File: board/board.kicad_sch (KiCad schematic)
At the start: 25 parts, among them J1 Conn_01x10_Pin, J2 Conn_01x10, J3 Conn_01x20, J4 Conn_01x02, J5 Conn_01x06, U1 nPM1300-CAXX, U2 ${ISP_PART}

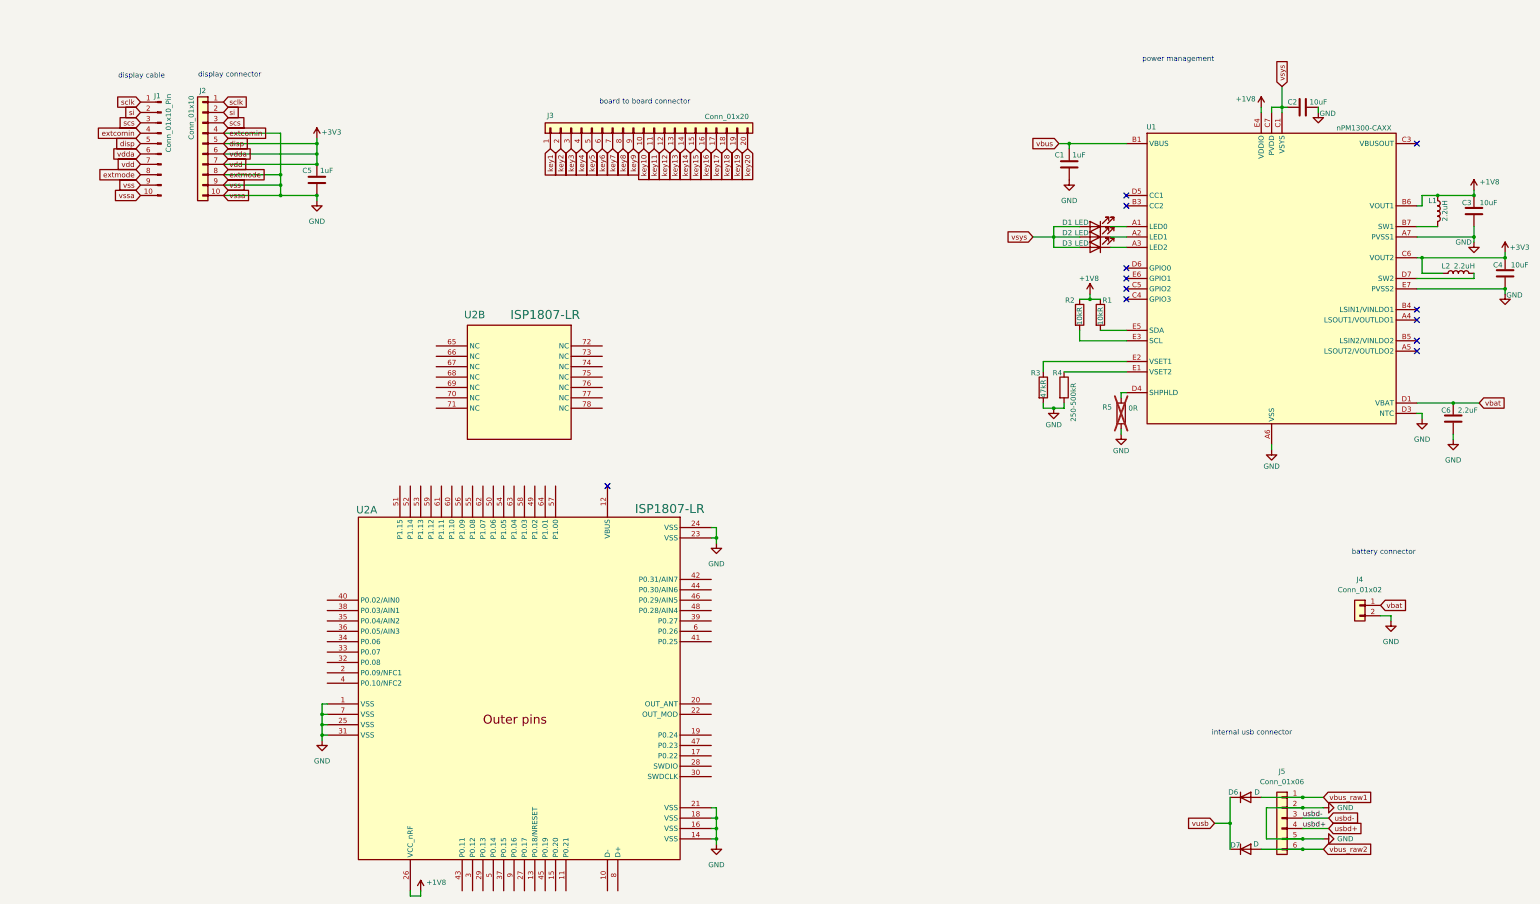
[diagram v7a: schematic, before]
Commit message: board: sch configure vusb
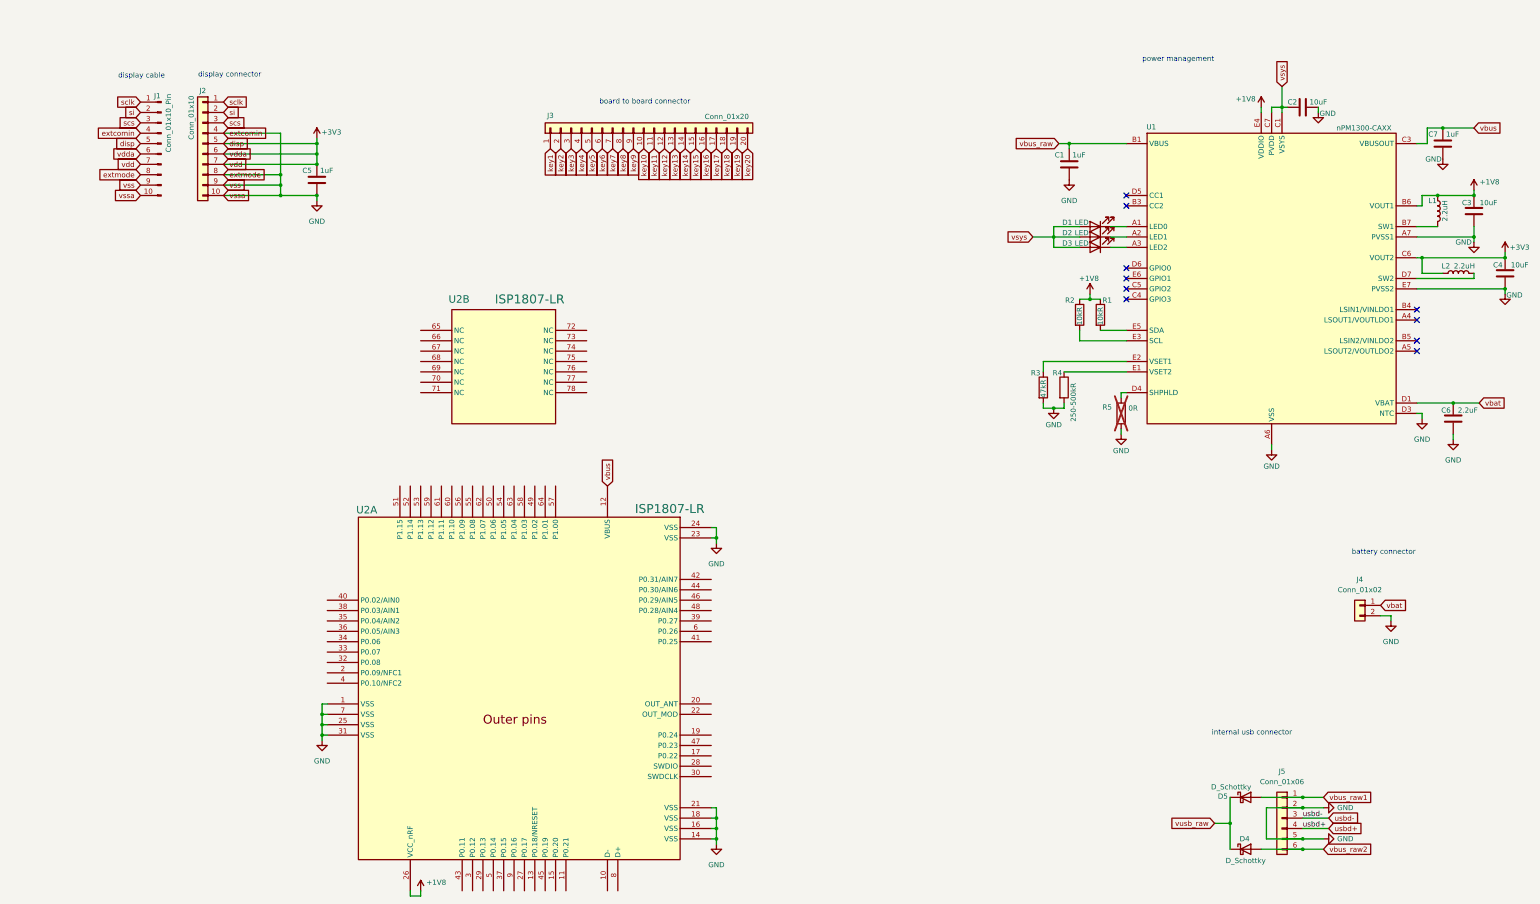
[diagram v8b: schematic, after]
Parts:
- removed D6, D7: D, symbol Device:D
- added C7: 1uF, symbol Device:C
- added D4, D5: D_Schottky, symbol Device:D_Schottky
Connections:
- net GND: now also C7.2
- net vbus: now also U1.C3 (VBUSOUT), U2.12 (VBUS), C7.1; no longer C1.1, U1.B1 (VBUS), U1.B2 (VBUS)
- net vbus_raw1: now also D5.2 (A)
- net vbus_raw2: now also D4.2 (A)
- new net vbus_raw: C1.1, U1.B1 (VBUS), U1.B2 (VBUS)
- new net vusb_raw: D4.1 (K), D5.1 (K)
- no-connect marks 12 -> 10
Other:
- moved on the sheet: U2B
